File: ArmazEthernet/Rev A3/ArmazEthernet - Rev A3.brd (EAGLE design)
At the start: 72 x 80 mm, 125 parts, among them J1 22-05-7028-02, P1 RB1-125BAG1A, T1 H1102FNL, T2 H1102FNL, U1 TC1264-3.3, U2 TC1264-1.8, U3 KSZ8995MA, U4 AT24C02C-SSHM-B, X1 NE8FAV, X2 NE8FAV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

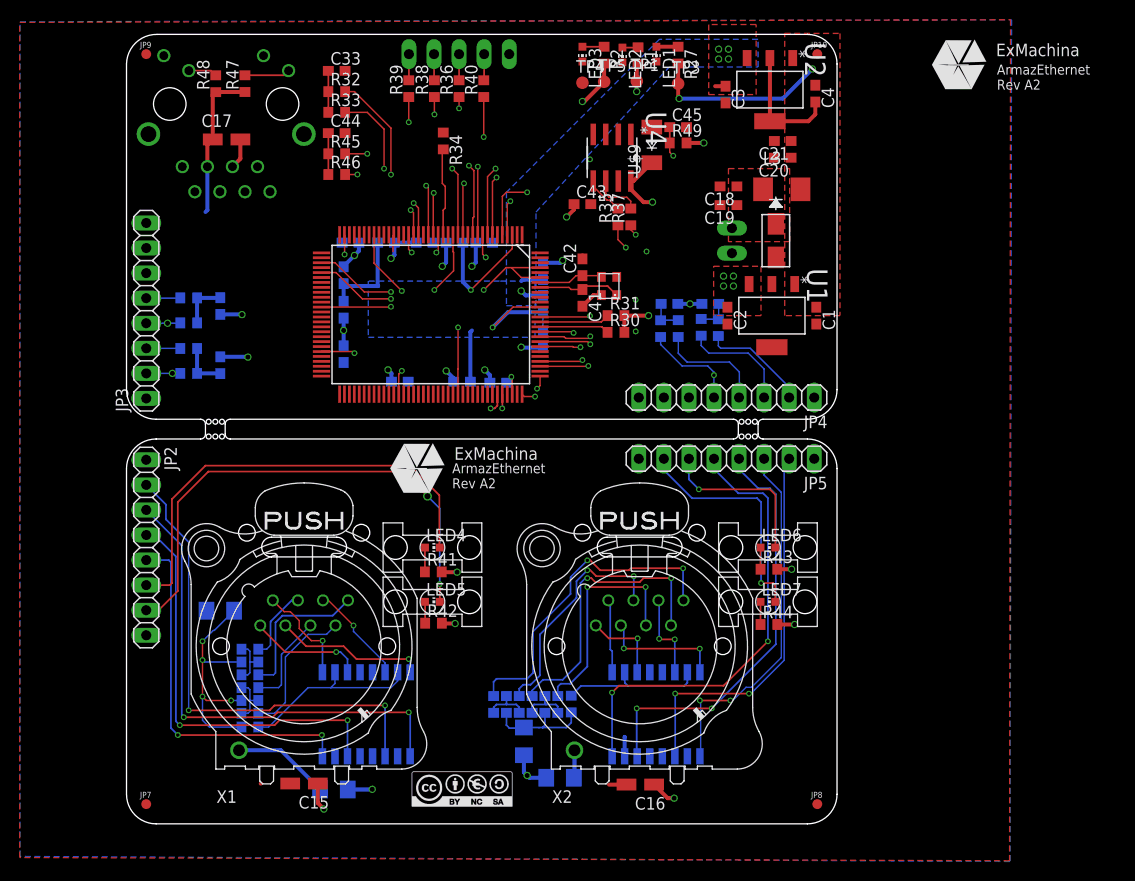
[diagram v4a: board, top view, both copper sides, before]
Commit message: Correctec the drc errors
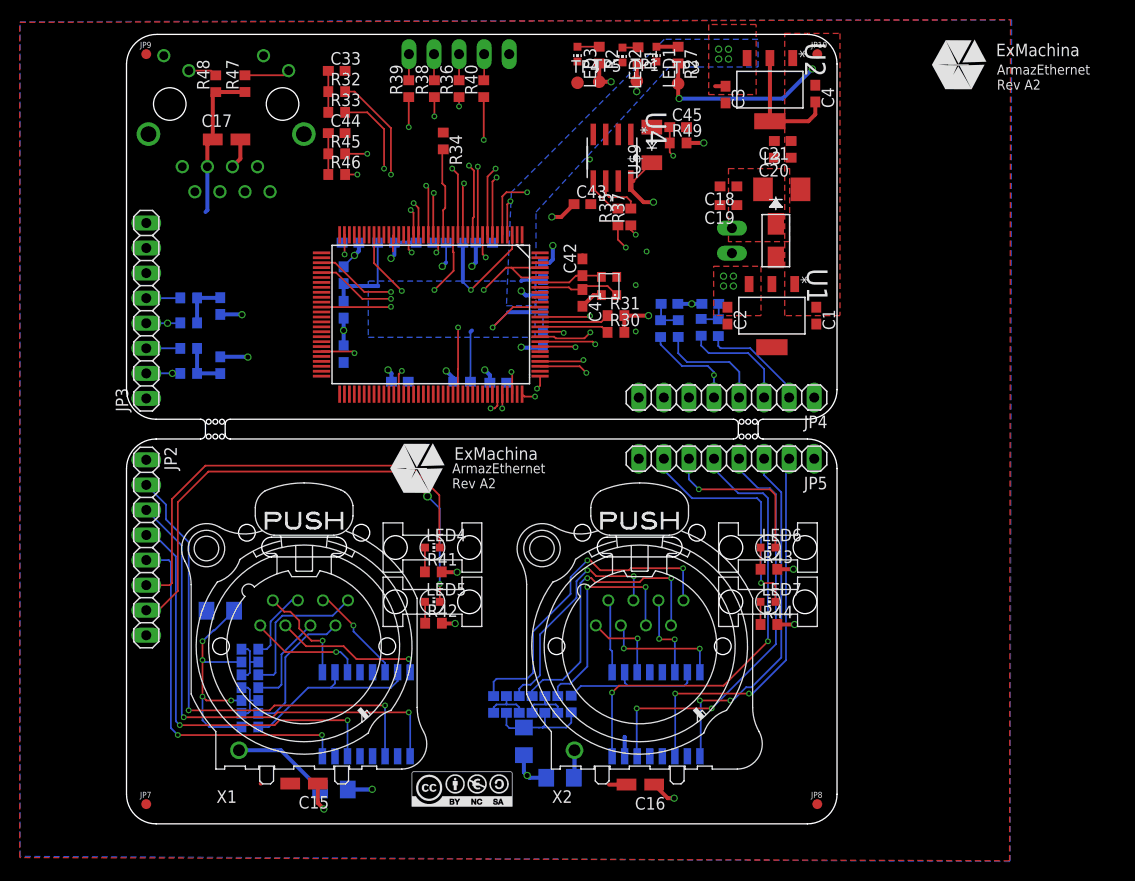
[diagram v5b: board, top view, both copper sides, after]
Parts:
- moved LED3 0.50 mm to (45.7, 78.0)
- moved R2 0.50 mm to (47.9, 77.9)
- moved TP4 0.50 mm to (45.7, 75.1)
- moved TP5 0.50 mm to (47.9, 75.2)
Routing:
- net SPIS-N: track 35.9 -> 34.0 mm
- net L2-1: track 33.7 -> 35.3 mm
- net L3-2: track 67.2 -> 65.7 mm
- net SPIQ: track 46.0 -> 45.0 mm
- net L1-2: track 101.6 -> 101.1 mm
- net L2-2: track 38.9 -> 39.5 mm

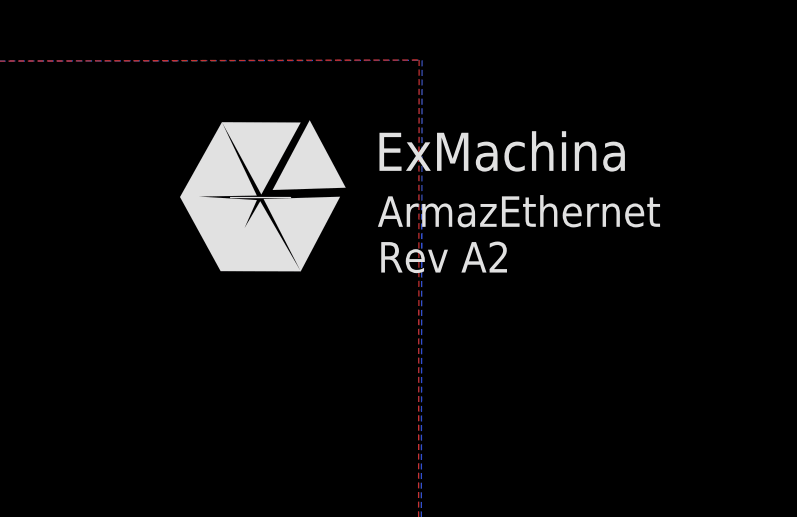
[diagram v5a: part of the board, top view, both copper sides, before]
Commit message: Add Exmachina logo and CC logo
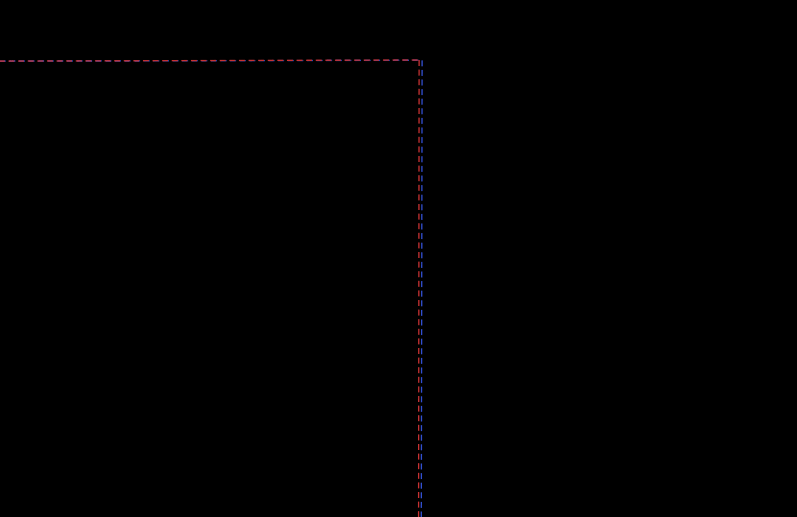
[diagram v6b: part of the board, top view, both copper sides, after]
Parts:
- moved U$5 32.9 mm to (52.1, 70.1), flipped to the bottom
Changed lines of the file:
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@@
 <layers>
 <layer number="1" name="Top" color="4" fill="1" visible="no" active="yes"/>
-<layer number="16" name="Bottom" color="1" fill="1" visible="no" active="yes"/>
+<layer number="16" name="Bottom" color="1" fill="1" visible="yes" active="yes"/>
 <layer number="17" name="Pads" color="2" fill="1" visible="yes" active="yes"/>
 <layer number="18" name="Vias" color="2" fill="1" visible="yes" active="yes"/>
 <layer number="19" name="Unrouted" color="6" fill="1" visible="yes" active="yes"/>
 <layer number="20" name="Dimension" color="15" fill="1" visible="yes" active="yes"/>
-<layer number="21" name="tPlace" color="7" fill="1" visible="yes" active="yes"/>
-<layer number="22" name="bPlace" color="7" fill="1" visible="no" active="yes"/>
-<layer number="23" name="tOrigins" color="15" fill="1" visible="yes" active="yes"/>
-<layer number="24" name="bOrigins" color="15" fill="1" visible="no" active="yes"/>
-<layer number="25" name="tNames" color="7" fill="1" visible="yes" active="yes"/>
-<layer number="26" name="bNames" color="7" fill="1" visible="no" active="yes"/>
-<layer number="27" name="tValues" color="7" fill="1" visible="yes" active="yes"/>
-<layer number="28" name="bValues" color="7" fill="1" visible="no" active="yes"/>
+<layer number="21" name="tPlace" color="7" fill="1" visible="no" active="yes"/>
+<layer number="22" name="bPlace" color="7" fill="1" visible="yes" active="yes"/>
+<layer number="23" name="tOrigins" color="15" fill="1" visible="no" active="yes"/>
+<layer number="24" name="bOrigins" color="15" fill="1" visible="yes" active="yes"/>
+<layer number="25" name="tNames" color="7" fill="1" visible="no" active="yes"/>
+<layer number="26" name="bNames" color="7" fill="1" visible="yes" active="yes"/>
+<layer number="27" name="tValues" color="7" fill="1" visible="no" active="yes"/>
+<layer number="28" name="bValues" color="7" fill="1" visible="yes" active="yes"/>
 <layer number="29" name="tStop" color="7" fill="3" visible="no" active="yes"/>
 <layer number="30" name="bStop" color="7" fill="6" visible="no" active="yes"/>
@@
 <layer number="49" name="Reference" color="7" fill="1" visible="no" active="yes"/>
 <layer number="50" name="dxf" color="7" fill="1" visible="no" active="yes"/>
-<layer number="51" name="tDocu" color="7" fill="1" visible="yes" active="yes"/>
+<layer number="51" name="tDocu" color="7" fill="1" visible="no" active="yes"/>
 <layer number="52" name="bDocu" color="7" fill="1" visible="no" active="yes"/>
 <layer number="91" name="Nets" color="2" fill="1" visible="no" active="no"/>
@@
 <layer number="96" name="Values" color="7" fill="1" visible="no" active="no"/>
 <layer number="2" name="Route2" color="38" fill="1" visible="no" active="yes"/>
-<layer number="3" name="Route3" color="16" fill="1" visible="yes" active="yes"/>
+<layer number="3" name="Route3" color="16" fill="1" visible="no" active="yes"/>
 <layer number="14" name="Route14" color="1" fill="6" visible="no" active="no"/>
 <layer number="15" name="Route15" color="4" fill="6" visible="no" active="no"/>
@@
 <hole x="62.325" y="39.25" drill="0.5"/>
 <hole x="63.675" y="39.25" drill="0.5"/>
-<text x="88.2" y="74.4" size="1.016" layer="21">ArmazEthernet
+<text x="48.5506" y="67.9992" size="1.016" layer="22" rot="MR0">ArmazEthernet
 Rev A2</text>
 <text x="33" y="34" size="1.016" layer="21">ArmazEthernet
@@
 <element name="U$3" library="mentor" package="1275.100" value="" x="31" y="28" rot="R180"/>
 <element name="U$4" library="mentor" package="1275.100" value="" x="31" y="22.5" rot="R180"/>
-<element name="U$5" library="exmachina" package="EXM-LOGO-BASELINE" value="EXMACHINA-LOGO-NAME" x="84.3" y="76.9">
-<attribute name="OC_NEWARK" value="unknown" x="84.3" y="76.9" size="1.778" layer="27" display="off"/>
-<attribute name="MF" value="" x="84.3" y="76.9" size="1.778" layer="27" display="off"/>
-<attribute name="MPN" value="" x="84.3" y="76.9" size="1.778" layer="27" display="off"/>
+<element name="U$5" library="exmachina" package="EXM-LOGO-BASELINE" value="EXMACHINA-LOGO-NAME" x="52.1182" y="70.1436" rot="MR0">
+<attribute name="OC_NEWARK" value="unknown" x="52.1182" y="70.1436" size="1.778" layer="28" rot="MR0" display="off"/>
+<attribute name="MF" value="" x="52.1182" y="70.1436" size="1.778" layer="28" rot="MR0" display="off"/>
+<attribute name="MPN" value="" x="52.1182" y="70.1436" size="1.778" layer="28" rot="MR0" display="off"/>
 </element>
 <element name="U$8" library="exmachina" package="EXM-LOGO-BASELINE" value="EXMACHINA-LOGO-NAME" x="29.4" y="36">

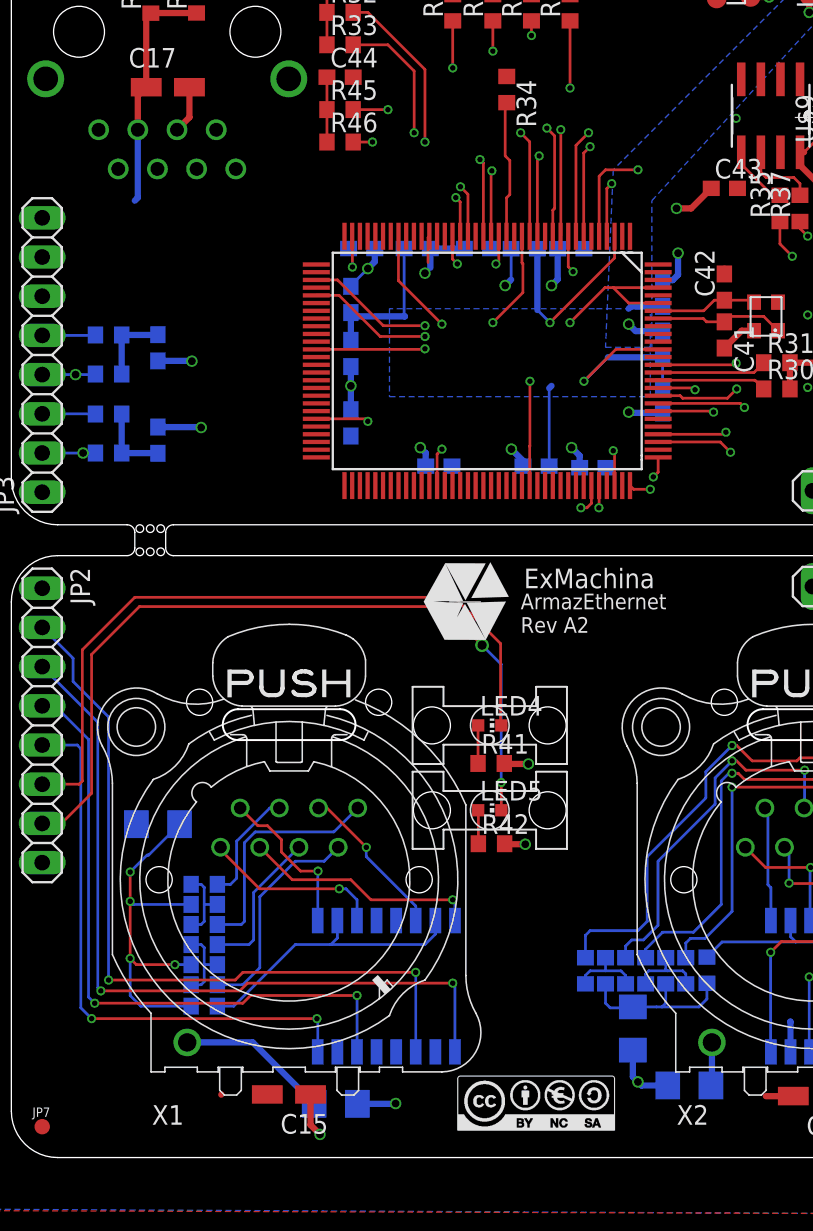
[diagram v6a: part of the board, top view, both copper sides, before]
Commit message: Update the placement of the logo and add seriegraphie of the test pads
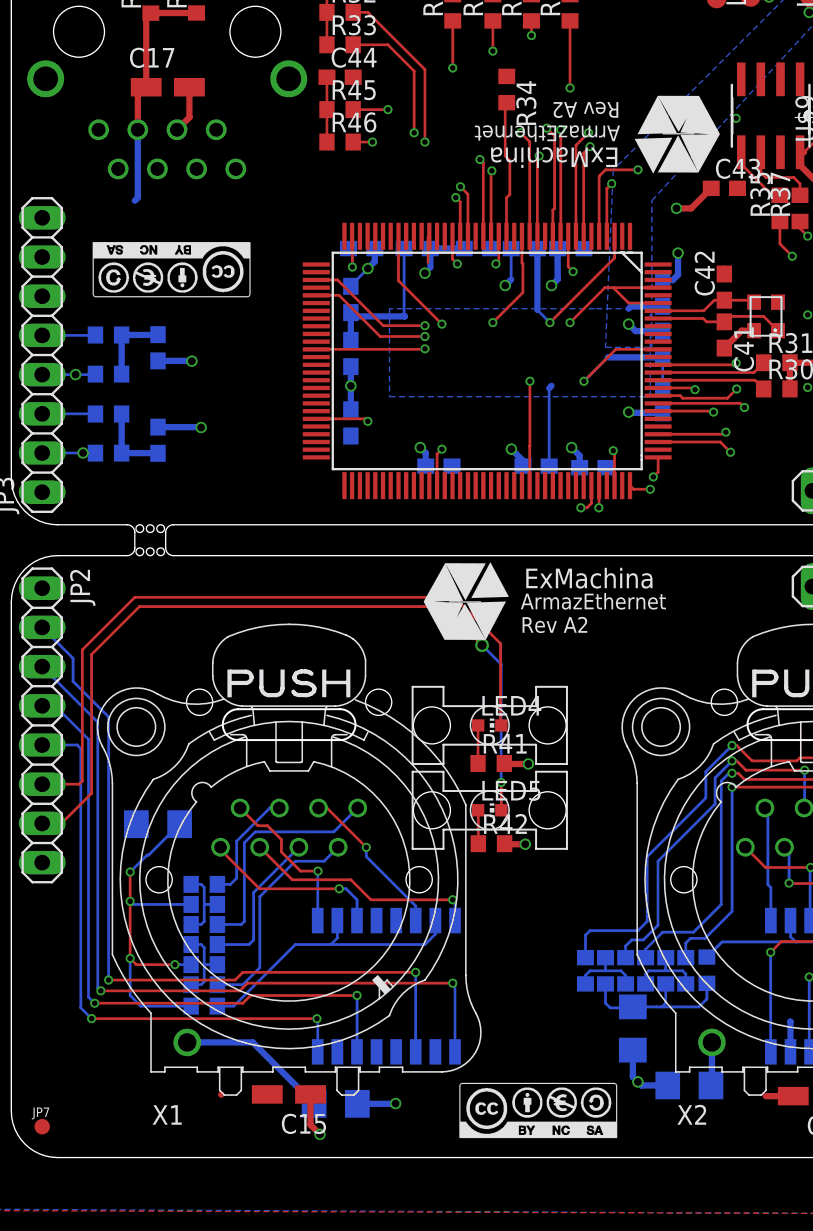
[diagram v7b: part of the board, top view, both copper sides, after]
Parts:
- added U$6: CC-BY-NC-SA, cc-by-sa:CC-BY-NC-SA
- moved U$5 9.67 mm to (43.2, 66.3), flipped to the top, turned to 180 degrees
- moved U$7 0.50 mm to (34.1, 3.02)
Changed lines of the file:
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@@
 <setting verticaltext="up"/>
 </settings>
-<grid distance="7" unitdist="mil" unit="mil" style="dots" multiple="1" display="yes" altdistance="0.1" altunitdist="mm" altunit="mm"/>
+<grid distance="1.27" unitdist="mm" unit="mil" style="dots" multiple="1" display="yes" altdistance="0.1" altunitdist="mm" altunit="mm"/>
 <layers>
-<layer number="1" name="Top" color="4" fill="1" visible="no" active="yes"/>
+<layer number="1" name="Top" color="4" fill="1" visible="yes" active="yes"/>
 <layer number="16" name="Bottom" color="1" fill="1" visible="yes" active="yes"/>
 <layer number="17" name="Pads" color="2" fill="1" visible="yes" active="yes"/>
@@
 <layer number="19" name="Unrouted" color="6" fill="1" visible="yes" active="yes"/>
 <layer number="20" name="Dimension" color="15" fill="1" visible="yes" active="yes"/>
-<layer number="21" name="tPlace" color="7" fill="1" visible="no" active="yes"/>
+<layer number="21" name="tPlace" color="7" fill="1" visible="yes" active="yes"/>
 <layer number="22" name="bPlace" color="7" fill="1" visible="yes" active="yes"/>
-<layer number="23" name="tOrigins" color="15" fill="1" visible="no" active="yes"/>
+<layer number="23" name="tOrigins" color="15" fill="1" visible="yes" active="yes"/>
 <layer number="24" name="bOrigins" color="15" fill="1" visible="yes" active="yes"/>
 <layer number="25" name="tNames" color="7" fill="1" visible="no" active="yes"/>
-<layer number="26" name="bNames" color="7" fill="1" visible="yes" active="yes"/>
+<layer number="26" name="bNames" color="7" fill="1" visible="no" active="yes"/>
 <layer number="27" name="tValues" color="7" fill="1" visible="no" active="yes"/>
-<layer number="28" name="bValues" color="7" fill="1" visible="yes" active="yes"/>
+<layer number="28" name="bValues" color="7" fill="1" visible="no" active="yes"/>
 <layer number="29" name="tStop" color="7" fill="3" visible="no" active="yes"/>
 <layer number="30" name="bStop" color="7" fill="6" visible="no" active="yes"/>
@@
 <layer number="49" name="Reference" color="7" fill="1" visible="no" active="yes"/>
 <layer number="50" name="dxf" color="7" fill="1" visible="no" active="yes"/>
-<layer number="51" name="tDocu" color="7" fill="1" visible="no" active="yes"/>
+<layer number="51" name="tDocu" color="7" fill="1" visible="yes" active="yes"/>
 <layer number="52" name="bDocu" color="7" fill="1" visible="no" active="yes"/>
 <layer number="91" name="Nets" color="2" fill="1" visible="no" active="no"/>
@@
 <layer number="95" name="Names" color="7" fill="1" visible="no" active="no"/>
 <layer number="96" name="Values" color="7" fill="1" visible="no" active="no"/>
-<layer number="2" name="Route2" color="38" fill="1" visible="no" active="yes"/>
+<layer number="2" name="Route2" color="38" fill="1" visible="yes" active="yes"/>
 <layer number="3" name="Route3" color="16" fill="1" visible="no" active="yes"/>
 <layer number="14" name="Route14" color="1" fill="6" visible="no" active="no"/>
@@
 <layer number="99" name="SpiceOrder" color="7" fill="1" visible="no" active="no"/>
 <layer number="100" name="Mechanical" color="7" fill="1" visible="no" active="no"/>
+<layer number="101" name="Patch_Top" color="7" fill="1" visible="no" active="yes"/>
 <layer number="102" name="Vscore" color="13" fill="1" visible="no" active="no"/>
 <layer number="103" name="Top_middle" color="7" fill="1" visible="no" active="no"/>
@@
 <hole x="62.325" y="39.25" drill="0.5"/>
 <hole x="63.675" y="39.25" drill="0.5"/>
-<text x="48.5506" y="67.9992" size="1.016" layer="22" rot="MR0">ArmazEthernet
+<text x="39.4494" y="68.3908" size="1.016" layer="21" rot="SR180">ArmazEthernet
 Rev A2</text>
 <text x="33" y="34" size="1.016" layer="21">ArmazEthernet
@@
 <element name="U$3" library="mentor" package="1275.100" value="" x="31" y="28" rot="R180"/>
 <element name="U$4" library="mentor" package="1275.100" value="" x="31" y="22.5" rot="R180"/>
-<element name="U$5" library="exmachina" package="EXM-LOGO-BASELINE" value="EXMACHINA-LOGO-NAME" x="52.1182" y="70.1436" rot="MR0">
-<attribute name="OC_NEWARK" value="unknown" x="52.1182" y="70.1436" size="1.778" layer="28" rot="MR0" display="off"/>
-<attribute name="MF" value="" x="52.1182" y="70.1436" size="1.778" layer="28" rot="MR0" display="off"/>
-<attribute name="MPN" value="" x="52.1182" y="70.1436" size="1.778" layer="28" rot="MR0" display="off"/>
+<element name="U$5" library="exmachina" package="EXM-LOGO-BASELINE" value="EXMACHINA-LOGO-NAME" x="43.2282" y="66.3336" rot="R180">
+<attribute name="OC_NEWARK" value="unknown" x="43.2282" y="66.3336" size="1.778" layer="27" rot="R180" display="off"/>
+<attribute name="MF" value="" x="43.2282" y="66.3336" size="1.778" layer="27" rot="R180" display="off"/>
+<attribute name="MPN" value="" x="43.2282" y="66.3336" size="1.778" layer="27" rot="R180" display="off"/>
 </element>
 <element name="U$8" library="exmachina" package="EXM-LOGO-BASELINE" value="EXMACHINA-LOGO-NAME" x="29.4" y="36">
@@
 <attribute name="MF" value="" x="38.9" y="76.2" size="1.778" layer="27" display="off"/>
 </element>
-<element name="U$7" library="cc-by-sa" package="CC-BY-NC-SA" value="CC-BY-NC-SA" x="34" y="3.5"/>
+<element name="U$6" library="cc-by-sa" package="CC-BY-NC-SA" value="CC-BY-NC-SA" x="10.3886" y="57.5564" rot="R180"/>
+<element name="U$7" library="cc-by-sa" package="CC-BY-NC-SA" value="CC-BY-NC-SA" x="34.1376" y="3.0226"/>
 </elements>
 <signals>
